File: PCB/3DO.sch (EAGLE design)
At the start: 7 parts, among them U1 SN74AHCT125N, U2 SN74AHCT125N

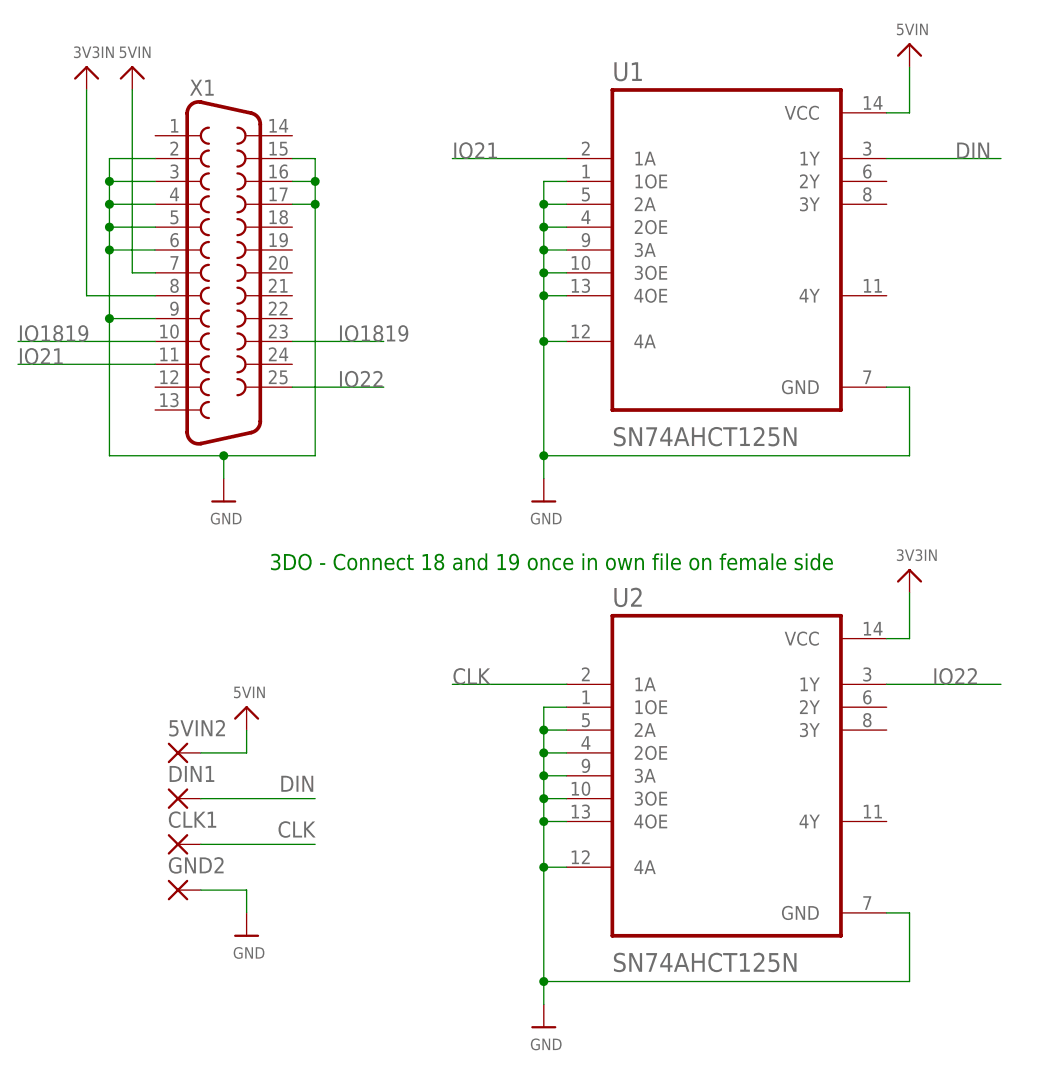
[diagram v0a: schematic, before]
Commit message: PCB Updates/New Additions
All existing PCBs had silkscreen updates and NES, Virtual Boy, PSX/PS2, Nintendo 64, Saturn have been added.
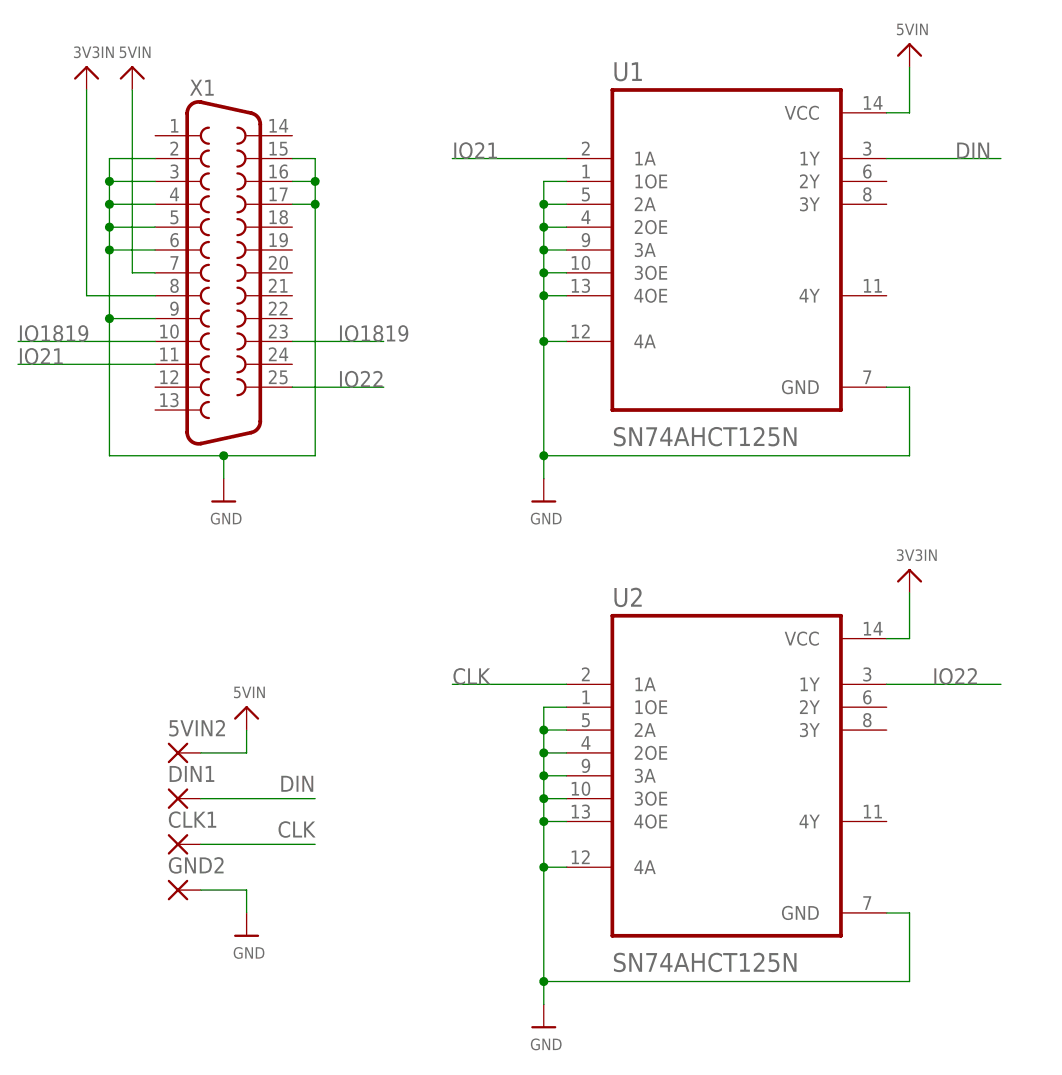
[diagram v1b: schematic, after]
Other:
- note removed: "3DO - Connect 18 and 19 once in own file on female side"
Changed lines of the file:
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@@
 <sheet>
 <plain>
-<text x="360.68" y="-121.92" size="1.778" layer="91">3DO - Connect 18 and 19 once in own file on female side</text>
 </plain>
 <instances>

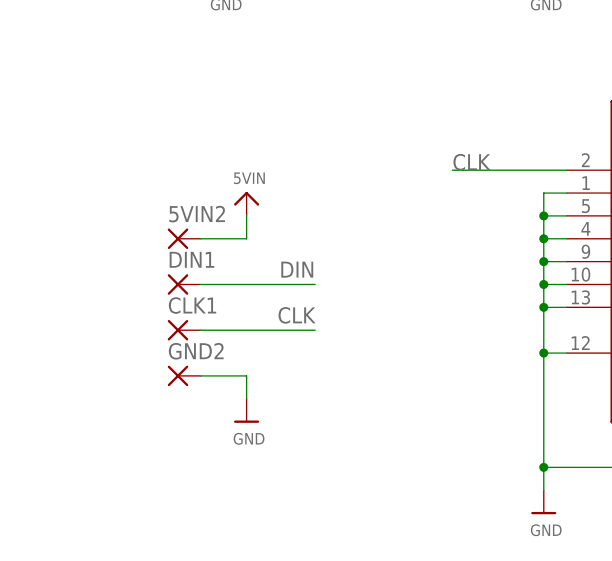
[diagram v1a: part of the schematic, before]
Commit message: PCB Update for better Housing Fit
All the PCBs were updated for better housing fitment.

Common Changes across all PCBs:
1. All Aux PCBs are now the exact same size.  (there was a .1mm-.5mm Variance previous)
2. All Aux PCBs Mounting holes are in the same location (there was a .05mm-.1mm Variance previous)
3. The DB25 has been moved 1.2mm close to the edge of the PCB for better connection when in the housing.

PCB Specific Updates:
3DO - Rename Pads (Removed trailing numbers), Flipped U2 to match U1, Moved U1 & U2 to same coordinates as other 2 Component PCBs in collection.

PCE & NES- Moved U1 & U2 to same coordinates as other 2 Component PCBs in collection.

PS2/PSX & Saturn - Added Notch on back edge of PCB for access for wires that need to attach to bottom layer of PCB.

All Gerbers have been updated.

New PCBs have been ordered for testing.
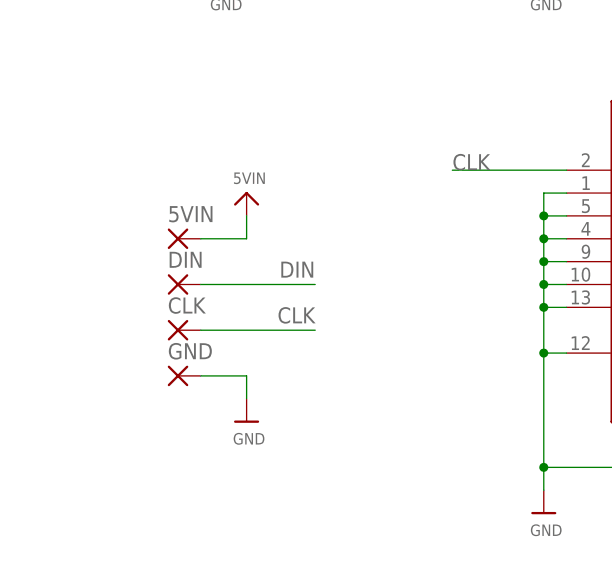
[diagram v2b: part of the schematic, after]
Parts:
- renumbered 5VIN2 to 5VIN, CLK1 to CLK, DIN1 to DIN, GND2 to GND
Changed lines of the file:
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@@
 <part name="U$41" library="Airquality_Sensor" library_urn="urn:adsk.eagle:library:16015176" deviceset="GND" device=""/>
 <part name="U$42" library="microbuilder" deviceset="VIN" device="" value="5VIN"/>
-<part name="5VIN2" library="wirepad" library_urn="urn:adsk.eagle:library:412" deviceset="SMD5" device="" package3d_urn="urn:adsk.eagle:package:30841/1"/>
-<part name="DIN1" library="wirepad" library_urn="urn:adsk.eagle:library:412" deviceset="SMD5" device="" package3d_urn="urn:adsk.eagle:package:30841/1"/>
-<part name="CLK1" library="wirepad" library_urn="urn:adsk.eagle:library:412" deviceset="SMD5" device="" package3d_urn="urn:adsk.eagle:package:30841/1"/>
-<part name="GND2" library="wirepad" library_urn="urn:adsk.eagle:library:412" deviceset="SMD5" device="" package3d_urn="urn:adsk.eagle:package:30841/1"/>
+<part name="5VIN" library="wirepad" library_urn="urn:adsk.eagle:library:412" deviceset="SMD5" device="" package3d_urn="urn:adsk.eagle:package:30841/1"/>
+<part name="DIN" library="wirepad" library_urn="urn:adsk.eagle:library:412" deviceset="SMD5" device="" package3d_urn="urn:adsk.eagle:package:30841/1"/>
+<part name="CLK" library="wirepad" library_urn="urn:adsk.eagle:library:412" deviceset="SMD5" device="" package3d_urn="urn:adsk.eagle:package:30841/1"/>
+<part name="GND" library="wirepad" library_urn="urn:adsk.eagle:library:412" deviceset="SMD5" device="" package3d_urn="urn:adsk.eagle:package:30841/1"/>
 </parts>
 <sheets>
@@
 <attribute name="VALUE" x="356.616" y="-136.144" size="1.27" layer="96"/>
 </instance>
-<instance part="5VIN2" gate="1" x="350.52" y="-142.24" smashed="yes">
+<instance part="5VIN" gate="1" x="350.52" y="-142.24" smashed="yes">
 <attribute name="NAME" x="349.377" y="-140.3858" size="1.778" layer="95"/>
 <attribute name="VALUE" x="349.377" y="-145.542" size="1.778" layer="96"/>
 </instance>
-<instance part="DIN1" gate="1" x="350.52" y="-147.32" smashed="yes">
+<instance part="DIN" gate="1" x="350.52" y="-147.32" smashed="yes">
 <attribute name="NAME" x="349.377" y="-145.4658" size="1.778" layer="95"/>
 <attribute name="VALUE" x="349.377" y="-150.622" size="1.778" layer="96"/>
 </instance>
-<instance part="CLK1" gate="1" x="350.52" y="-152.4" smashed="yes">
+<instance part="CLK" gate="1" x="350.52" y="-152.4" smashed="yes">
 <attribute name="NAME" x="349.377" y="-150.5458" size="1.778" layer="95"/>
 <attribute name="VALUE" x="349.377" y="-155.702" size="1.778" layer="96"/>
 </instance>
-<instance part="GND2" gate="1" x="350.52" y="-157.48" smashed="yes">
+<instance part="GND" gate="1" x="350.52" y="-157.48" smashed="yes">
 <attribute name="NAME" x="349.377" y="-155.6258" size="1.778" layer="95"/>
 <attribute name="VALUE" x="349.377" y="-160.782" size="1.778" layer="96"/>
@@
 </segment>
 <segment>
-<pinref part="GND2" gate="1" pin="P"/>
+<pinref part="GND" gate="1" pin="P"/>
 <wire x1="353.06" y1="-157.48" x2="358.14" y2="-157.48" width="0.1524" layer="91"/>
 <pinref part="U$41" gate="G$1" pin="GND"/>
@@
 </segment>
 <segment>
-<pinref part="5VIN2" gate="1" pin="P"/>
+<pinref part="5VIN" gate="1" pin="P"/>
 <pinref part="U$42" gate="G$1" pin="VIN"/>
 <wire x1="353.06" y1="-142.24" x2="358.14" y2="-142.24" width="0.1524" layer="91"/>
@@
 <wire x1="353.06" y1="-152.4" x2="365.76" y2="-152.4" width="0.1524" layer="91"/>
 <label x="365.76" y="-149.86" size="1.778" layer="95" rot="R180"/>
-<pinref part="CLK1" gate="1" pin="P"/>
+<pinref part="CLK" gate="1" pin="P"/>
 </segment>
 </net>
@@
 <wire x1="353.06" y1="-147.32" x2="365.76" y2="-147.32" width="0.1524" layer="91"/>
 <label x="365.76" y="-144.78" size="1.778" layer="95" rot="R180"/>
-<pinref part="DIN1" gate="1" pin="P"/>
-</segment>
-</net>
+<pinref part="DIN" gate="1" pin="P"/>
+</segment>
+</net>

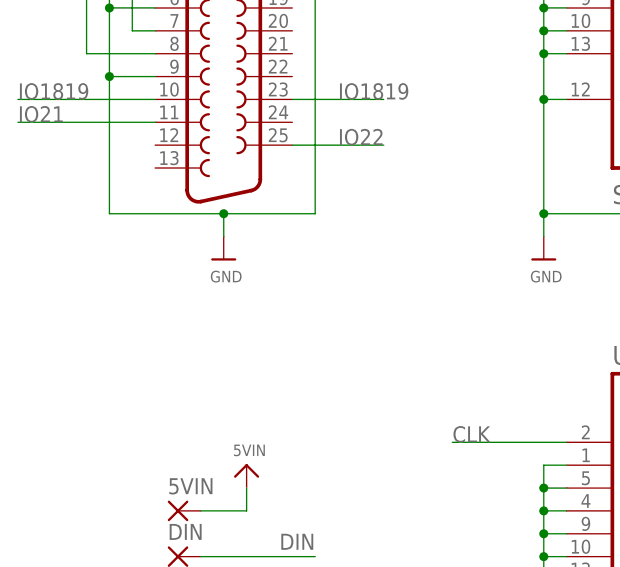
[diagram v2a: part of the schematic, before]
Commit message: Added exposed GND plane at DB25 anchors
All PCBs have been update to have exposed GND plane pads for the DB25 anchor points.

This resolves Issue 54
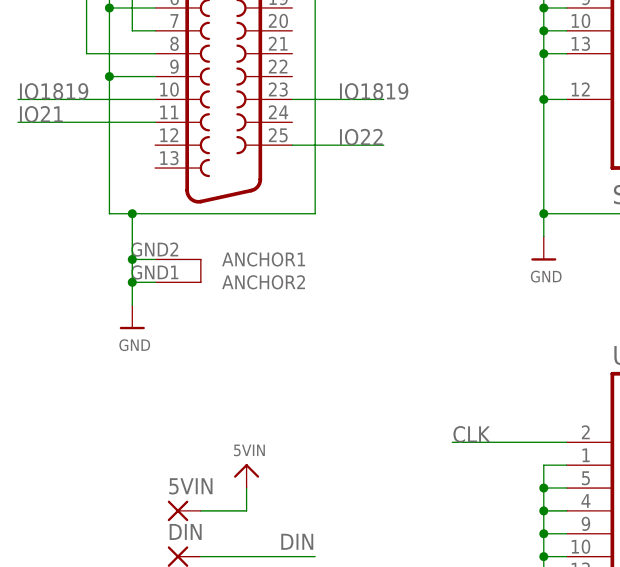
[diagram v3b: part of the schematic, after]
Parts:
- X1: device SparkFun-Retired:DB25_FEMALEH -> SparkFun-Retired:DB25_FEMALEHP
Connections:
- net GND: now also X1.ANCHOR1, X1.ANCHOR2
